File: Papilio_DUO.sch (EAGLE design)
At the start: 110 parts, among them IC1 FT2232H, SW1 SWITCH-2CH-6P-3010010P1, SW2 EVQQ2, U1 ARDUINO_MEGA_SHIELD, U101 ATMEGA32U4-XUMU, U2 LTC3419EMS, U3 93C46B, X1 12MHz, Y1 16MHz KX-7

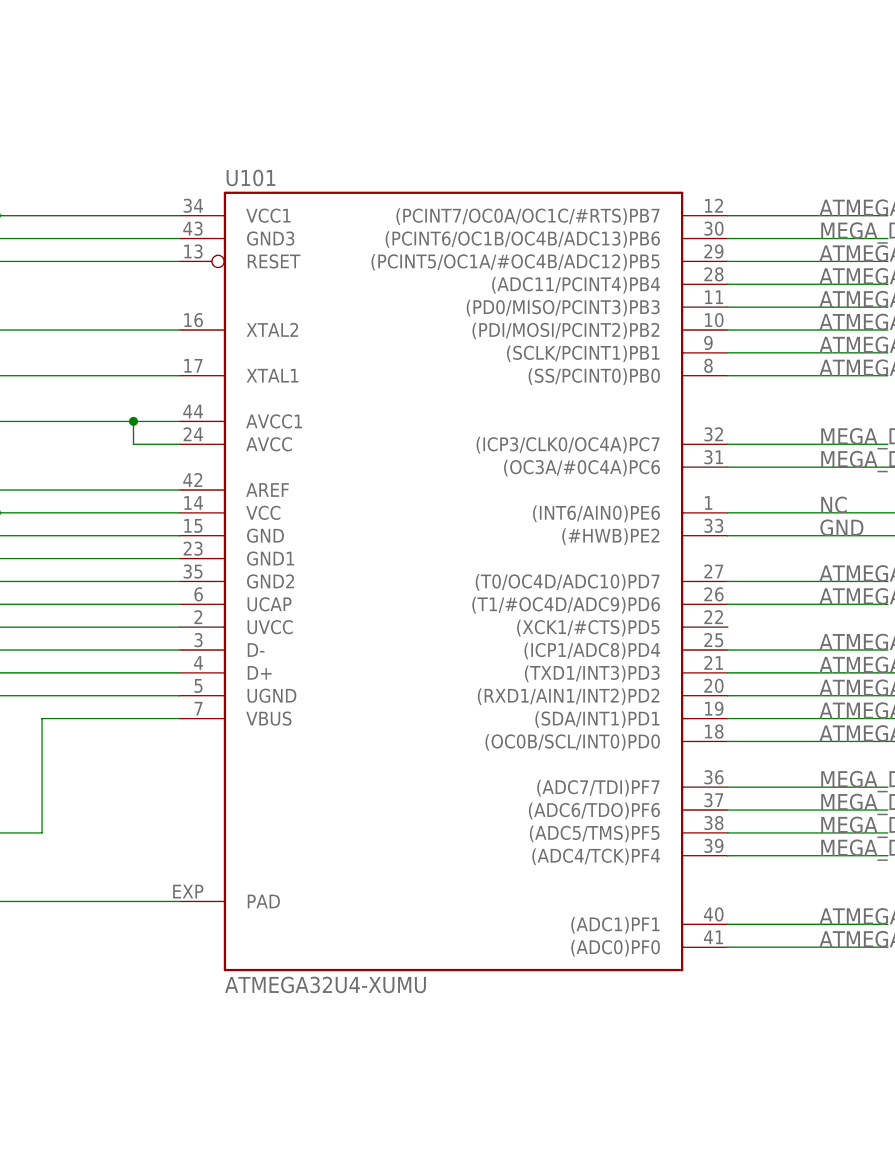
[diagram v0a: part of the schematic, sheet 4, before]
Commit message: Added TQFP footprint
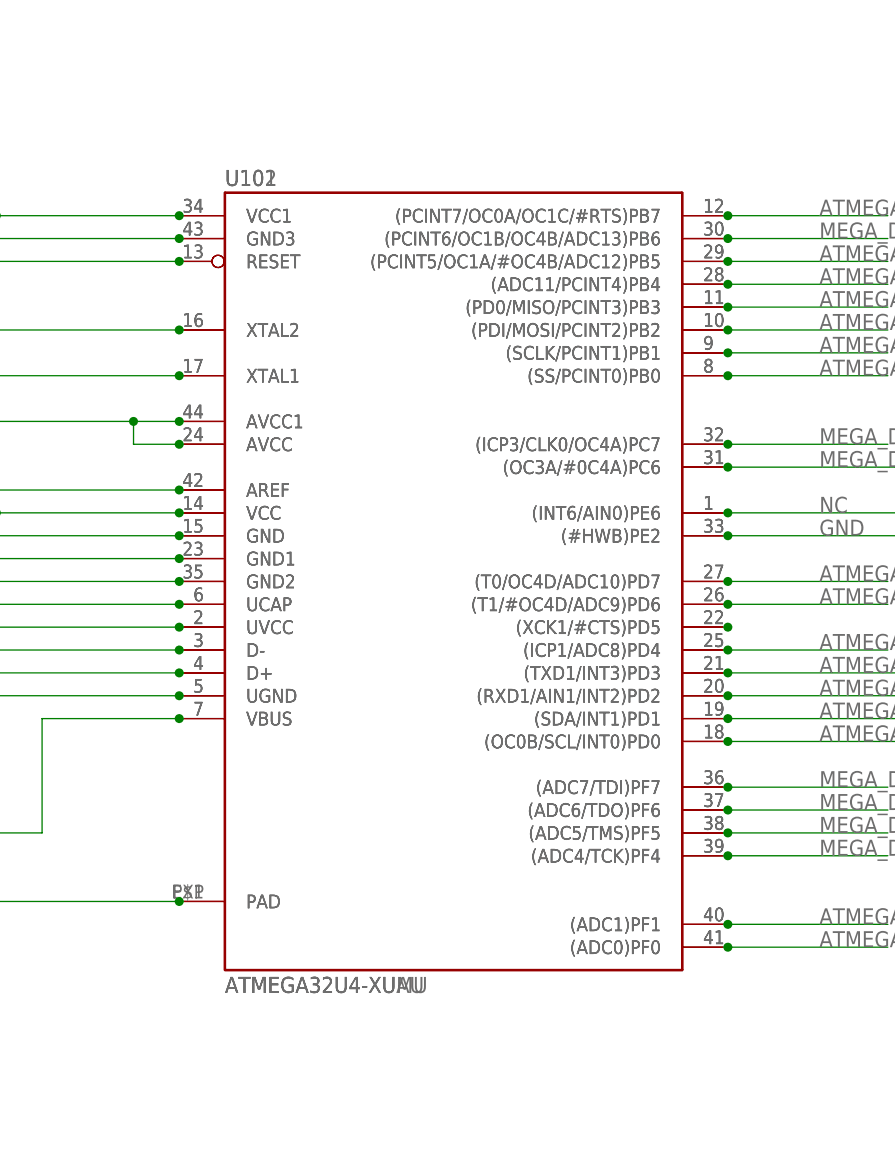
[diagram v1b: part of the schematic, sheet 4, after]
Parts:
- added U102: ATMEGA32U4-XUAU, SmartPrj:ATMEGA32U4-XUAU
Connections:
- new net N$1: U101.(XCK1/#CTS)PD5, U102.(XCK1/#CTS)PD5
- net 3V3: now also U102.UVCC, U102.VCC, U102.VCC1
- net 5V_ARDUINO: now also U102.VBUS
- net ARD_RESET: now also U102.RESET
- net AREF: now also U102.AREF
- net ATMEGA_A0: now also U102.(ADC0)PF0
- net ATMEGA_A1: now also U102.(ADC1)PF1
- net ATMEGA_D0/RX: now also U102.(RXD1/AIN1/INT2)PD2
- net ATMEGA_D1/TX: now also U102.(TXD1/INT3)PD3
- net ATMEGA_D2: now also U102.(PCINT5/OC1A/#OC4B/ADC12)PB5
- net ATMEGA_D3: now also U102.(ADC11/PCINT4)PB4
- net ATMEGA_D4: now also U102.(T0/OC4D/ADC10)PD7
- net ATMEGA_D5*: now also U102.(T1/#OC4D/ADC9)PD6
- net ATMEGA_D6*: now also U102.(ICP1/ADC8)PD4
- net ATMEGA_D7: now also U102.(SDA/INT1)PD1
- net ATMEGA_IO10*: now also U102.(SS/PCINT0)PB0
- net ATMEGA_IO11*: now also U102.(PDI/MOSI/PCINT2)PB2
- net ATMEGA_IO12: now also U102.(PD0/MISO/PCINT3)PB3
- net ATMEGA_IO13*: now also U102.(SCLK/PCINT1)PB1
- net ATMEGA_IO8: now also U102.(OC0B/SCL/INT0)PD0
- net ATMEGA_IO9*: now also U102.(PCINT7/OC0A/OC1C/#RTS)PB7
- net AVCC: now also U102.AVCC, U102.AVCC1
- net AVRUSB_N: now also U102.D-
- net AVRUSB_P: now also U102.D+
- net GND: now also U102.(#HWB)PE2, U102.GND, U102.GND1, U102.GND2, U102.GND3, U102.PAD, U102.UGND
- net MEGA_D14: now also U102.(PCINT6/OC1B/OC4B/ADC13)PB6
- net MEGA_D15: now also U102.(OC3A/#0C4A)PC6
- net MEGA_D16: now also U102.(ICP3/CLK0/OC4A)PC7
- net MEGA_D28/A5: now also U102.(ADC7/TDI)PF7
- net MEGA_D30/A4: now also U102.(ADC6/TDO)PF6
- net MEGA_D32/A3: now also U102.(ADC5/TMS)PF5
- net MEGA_D34/A2: now also U102.(ADC4/TCK)PF4
- net NC: now also U102.(INT6/AIN0)PE6
- net UCAP: now also U102.UCAP
- net XTAL1: now also U102.XTAL1
- net XTAL2: now also U102.XTAL2

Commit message: Version 1.5 - Kickstarter Edition
-Added TQFP footprint for the ATmega32U4
-Changed values for LED resistors so they won't be so bright. R7, R29,
R30
-Changed size of the EEPROM used by the FT2232H chip from 1K to 2K. This
allows us to look like official Xilinx Cable. U3
-Fixed up some silkscreen markings to make it more obvious how to place
the parts.
-Added the Kickstarter Special Edition Marking
-Changed PCB color to Black
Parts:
- C101, C102, C103, C104, C105, C106, C107: device SmartPrj:C-EUC0603K -> GadgetFactory:C0603
- LED: device led:LEDCHIPLED_0805 -> led:LEDCHIP-LED0805
- R109: device SmartPrj:R-EU_R0603 -> GadgetFactory:R0603
- R23, R24, R25, R26, R27, R28: device dp_devices:RESISTORR603 -> GadgetFactory:R0603
- R29, R30: value 470 -> 1K; device dp_devices:RESISTORR603 -> GadgetFactory:R0603
- R7: value 1K -> 4.7K
- RX, TX: device dp_devices:LED805 -> led:LEDCHIP-LED0805
- U3: value 93C46B -> 93C56B
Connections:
- net !RESET: now also R28A.2; no longer R28.2
- net 3V3: now also R23A.2, R24A.2, R26A.2, R28A.1; no longer R23.2, R24.2, R26.2, R28.1
- net BC3: now also R30A.1; no longer R30.1
- net BC4: now also R29A.1; no longer R29.1
- net EECLK: now also R24A.1; no longer R24.1
- net EECS: now also R23A.1; no longer R23.1
- net EEDATA: now also R25A.2; no longer R25.2
- net GND: now also R27A.1; no longer R27.1
- net N$24: now also R30A.2; no longer R30.2
- net N$25: now also R29A.2; no longer R29.2
- net N$45: now also R25A.1, R26A.1; no longer R25.1, R26.1
- net N$9: now also R27A.2; no longer R27.2
- net XTAL1: now also R109A.1; no longer R109.1
- net XTAL2: now also R109A.2; no longer R109.2
